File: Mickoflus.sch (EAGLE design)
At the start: 46 parts, among them IC1 74HC595D, IC2 74HC595D

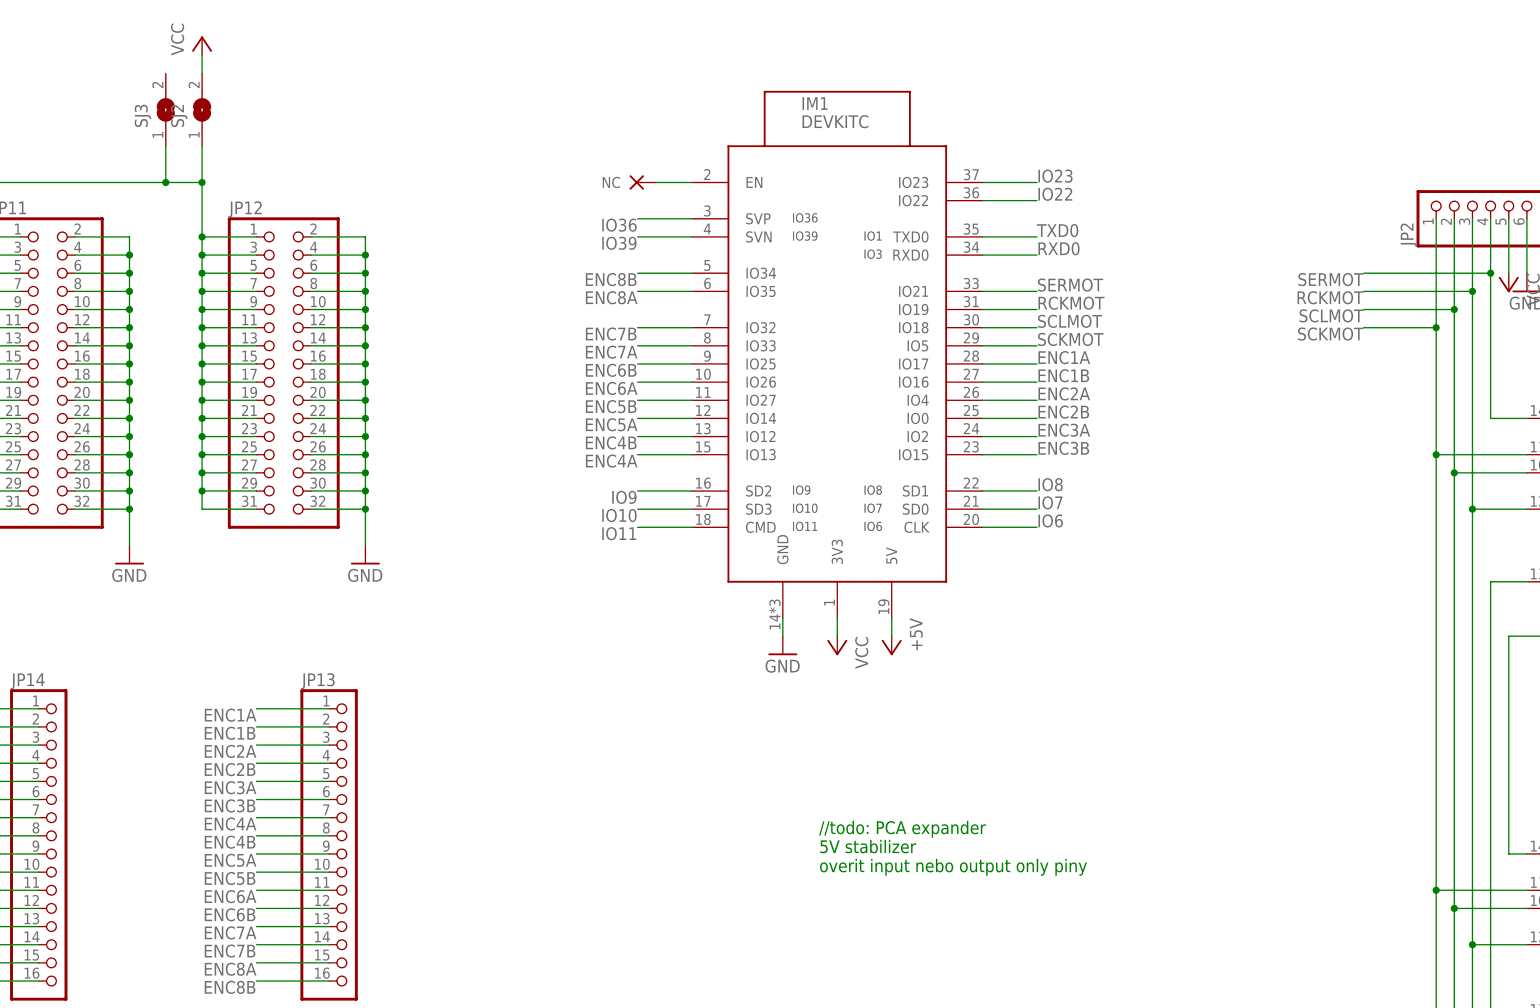
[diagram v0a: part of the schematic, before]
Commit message: Added 5V supply (still no stabilizer from battery to 5V).
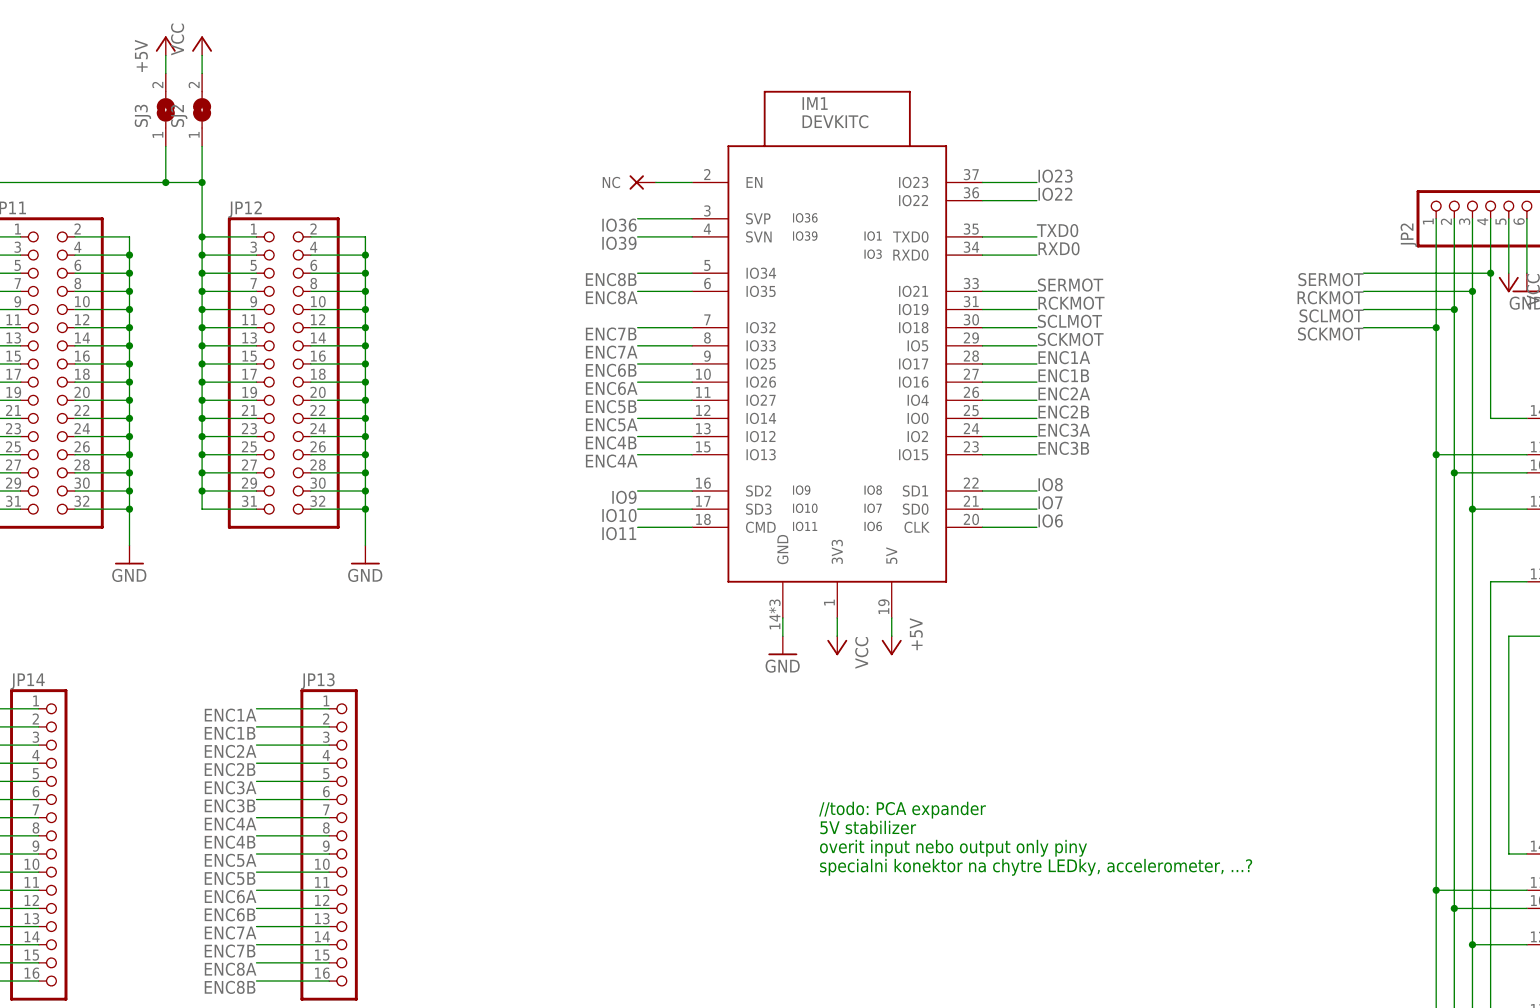
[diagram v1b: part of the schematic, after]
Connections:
- net +5V: now also SJ3.2
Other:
- note added: "//todo: PCA expander 5V stabilizer overit input nebo output only piny specialni konektor na chytre LEDky, accelerometer, ...?"
- note removed: "//todo: PCA expander 5V stabilizer overit input nebo output only piny"
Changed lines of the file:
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@@
 <part name="JP14" library="pinhead" deviceset="PINHD-1X16" device=""/>
 <part name="P+17" library="supply1" deviceset="+5V" device=""/>
+<part name="P+16" library="supply1" deviceset="+5V" device=""/>
 </parts>
 <sheets>
@@
 <text x="-121.92" y="22.86" size="1.778" layer="91">//todo: PCA expander
 5V stabilizer
-overit input nebo output only piny</text>
+overit input nebo output only piny
+specialni konektor na chytre LEDky, accelerometer, ...?</text>
 </plain>
 <instances>
@@
 <instance part="JP14" gate="A" x="-228.6" y="27.94"/>
 <instance part="P+17" gate="1" x="-111.76" y="53.34" rot="R180"/>
+<instance part="P+16" gate="1" x="-213.36" y="139.7"/>
 </instances>
 <busses>
@@
 <wire x1="-111.76" y1="55.88" x2="-111.76" y2="58.42" width="0.1524" layer="91"/>
 </segment>
-</net>
+<segment>
+<pinref part="SJ3" gate="1" pin="2"/>
+<pinref part="P+16" gate="1" pin="+5V"/>
+<wire x1="-213.36" y1="134.62" x2="-213.36" y2="137.16" width="0.1524" layer="91"/>
+</segment>
+</net>

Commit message: Major schematic improvements changed power supply names: VCC -> +3V3, V+ -> VCC fixed encoder power (+3V3 -> +5V) changed ESP pinout (disconnected internal memory pins, moved encoders out of bootstrap pins) ESP reset also resets motors drivers
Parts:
- removed NC1, NC2, NC3, NC4, NC8: NC, NC:NC
- added C1, C2: 100n, rcl_upravena:C-EUC1206
- added D1: (no value), diode:DIODE-0805
- added JP15, JP16, JP17, JP18: (no value), pinhead:PINHD-1X1
- added NC10, NC11, NC5, NC6, NC7, NC9: NC, NC:NC
- added Q1: (no value), transistors:N-MOSFET-SOT23-GSD
- added R1, R2, R3: 10k, rcl_upravena:R-EU_R1206
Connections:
- removed net IO10: IM1.SD3, JP14.7
- removed net IO11: IM1.CMD, JP14.8
- removed net IO6: IM1.CLK, JP14.3
- removed net IO7: IM1.SD0, JP14.4
- removed net IO8: IM1.SD1, JP14.5
- removed net IO9: IM1.SD2, JP14.6
- removed net N$104: NC1.NC, U$4.ULT
- removed net N$105: NC2.NC, U$3.ULT
- removed net N$106: NC3.NC, U$2.ULT
- removed net N$107: NC8.NC, U$1.ULT
- removed net N$56: IM1.EN, NC4.NC
- removed net SCLMOT: IC1A.SCL, IC2A.SCL, IM1.IO18, JP2.2, JP3.5
- removed net V+: POWER1-1.KL, POWER2-1.KL, U$1.VCC, U$2.VCC, U$3.VCC, U$4.VCC
- new net !FAULT0: JP15.1, U$1.ULT
- new net !FAULT1: JP16.1, U$2.ULT
- new net !FAULT2: JP17.1, U$3.ULT
- new net !FAULT3: JP18.1, U$4.ULT
- new net +3V3: C1.1, C2.1, IC1P.VCC, IC2P.VCC, IM1.3V3, JP2.6, JP3.1, Q1.G, R1.2, R3.2, SJ2.2
- new net EN: IC1A.SCL, IC2A.SCL, IM1.EN, JP2.2, JP3.5, Q1.S, R3.1, U$1.!SLEEP, U$2.!SLEEP, U$3.!SLEEP, U$4.!SLEEP
- new net IO10_NC: IM1.SD3, NC6.NC
- new net IO11_NC: IM1.CMD, NC7.NC
- new net IO21: IM1.IO21
- new net IO6_NC: IM1.CLK, NC9.NC
- new net IO7_NC: IM1.SD0, NC10.NC
- new net IO8_NC: IM1.SD1, NC11.NC
- new net IO9_NC: IM1.SD2, NC5.NC
- new net _EN_: D1.C, Q1.D
- net +5V: now also JP1.4, JP10.4, JP4.4, JP5.4, JP6.4, JP7.4, JP8.4, JP9.4
- net ENC1A: now also IM1.IO19; no longer IM1.IO17
- net ENC1B: now also IM1.IO18; no longer IM1.IO16
- net ENC2A: now also IM1.IO5; no longer IM1.IO4
- net ENC2B: now also IM1.IO17; no longer IM1.IO0
- net ENC3A: now also IM1.IO16; no longer IM1.IO2
- net ENC3B: now also IM1.IO4; no longer IM1.IO15
- net GND: now also C1.2, C2.2, IC1P.GND, IC2P.GND, JP1.3, JP10.3, JP2.5, JP3.2, JP4.3, JP5.3, JP6.3, JP7.3, JP8.3, JP9.3, R2.1; no longer JP1.4, JP10.4, JP2.6, JP3.1, JP4.4, JP5.4, JP6.4, JP7.4, JP8.4, JP9.4
- net RCKMOT: now also D1.A, IM1.IO0, R1.1; no longer IM1.IO19
- net SCKMOT: now also IM1.IO15; no longer IM1.IO5
- net SERMOT: now also IM1.IO2, R2.2; no longer IM1.IO21
- net VCC: now also POWER1-1.KL, POWER2-1.KL, U$1.VCC, U$2.VCC, U$3.VCC, U$4.VCC; no longer IM1.3V3, JP1.3, JP10.3, JP2.5, JP3.2, JP4.3, JP5.3, JP6.3, JP7.3, JP8.3, JP9.3, SJ2.2, U$1.!SLEEP, U$2.!SLEEP, U$3.!SLEEP, U$4.!SLEEP
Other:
- note added: "MUSI BYT ZDE!"
- moved on the sheet: IM1, JP11, JP12, JP13, JP14, JP3, SJ2, SJ3

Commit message: Added voltage regulator and IO expander.
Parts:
- added D2: 1N4004, diode:1N4004
- added IC4: (no value), v-reg:78XXS
- added JP19: (no value), pinhead:PINHD-1X4
- added R4, R5: (no value), resistor:R-EU_R1206
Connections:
- new net N$5: D2.C, IC4.IN
- new net SCL: IM1.IO22, JP19.1, R4.1
- new net SDA: IM1.IO23, JP19.2, R5.1
- net +3V3: now also JP19.3, R4.2, R5.2
- net +5V: now also IC4.OUT
- net GND: now also IC4.GND, JP19.4
- net IO22: no longer IM1.IO22
- net IO23: no longer IM1.IO23
- net VCC: now also D2.A
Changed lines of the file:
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@@
 <?xml version="1.0" encoding="utf-8"?>
 <!DOCTYPE eagle SYSTEM "eagle.dtd">
-<eagle version="7.7.0">
+<eagle version="6.5.0">
 <drawing>
 <settings>
@@
 <part name="JP17" library="pinhead" deviceset="PINHD-1X1" device=""/>
 <part name="JP18" library="pinhead" deviceset="PINHD-1X1" device=""/>
+<part name="IC4" library="v-reg" deviceset="78XXS" device=""/>
+<part name="GND30" library="supply1" deviceset="GND" device=""/>
+<part name="P+12" library="supply1" deviceset="VCC" device=""/>
+<part name="P+13" library="supply1" deviceset="+5V" device=""/>
+<part name="D2" library="diode" deviceset="1N4004" device=""/>
+<part name="JP19" library="pinhead" deviceset="PINHD-1X4" device=""/>
+<part name="GND29" library="supply1" deviceset="GND" device=""/>
+<part name="+3V9" library="supply1" deviceset="+3V3" device=""/>
+<part name="R4" library="resistor" deviceset="R-EU_" device="R1206"/>
+<part name="R5" library="resistor" deviceset="R-EU_" device="R1206"/>
+<part name="+3V10" library="supply1" deviceset="+3V3" device=""/>
 </parts>
 <sheets>
@@
 <instance part="JP17" gate="G$1" x="109.22" y="33.02"/>
 <instance part="JP18" gate="G$1" x="109.22" y="2.54"/>
+<instance part="IC4" gate="1" x="-137.16" y="12.7"/>
+<instance part="GND30" gate="1" x="-137.16" y="0"/>
+<instance part="P+12" gate="VCC" x="-170.18" y="20.32"/>
+<instance part="P+13" gate="1" x="-124.46" y="20.32"/>
+<instance part="D2" gate="1" x="-157.48" y="12.7"/>
+<instance part="JP19" gate="A" x="-132.08" y="-20.32"/>
+<instance part="GND29" gate="1" x="-142.24" y="-27.94"/>
+<instance part="+3V9" gate="G$1" x="-142.24" y="-7.62"/>
+<instance part="R4" gate="G$1" x="-193.04" y="-7.62" rot="R90"/>
+<instance part="R5" gate="G$1" x="-187.96" y="-7.62" rot="R90"/>
+<instance part="+3V10" gate="G$1" x="-190.5" y="5.08"/>
 </instances>
 <busses>
@@
 <wire x1="-63.5" y1="78.74" x2="-63.5" y2="81.28" width="0.1524" layer="91"/>
 </segment>
+<segment>
+<pinref part="GND30" gate="1" pin="GND"/>
+<pinref part="IC4" gate="1" pin="GND"/>
+<wire x1="-137.16" y1="2.54" x2="-137.16" y2="5.08" width="0.1524" layer="91"/>
+</segment>
+<segment>
+<pinref part="GND29" gate="1" pin="GND"/>
+<pinref part="JP19" gate="A" pin="4"/>
+<wire x1="-142.24" y1="-25.4" x2="-142.24" y2="-22.86" width="0.1524" layer="91"/>
+<wire x1="-142.24" y1="-22.86" x2="-134.62" y2="-22.86" width="0.1524" layer="91"/>
+</segment>
 </net>
 <net name="N$2" class="0">
@@
 <net name="IO23" class="0">
 <segment>
-<pinref part="IM1" gate="G$1" pin="IO23"/>
-<wire x1="-114.3" y1="111.76" x2="-106.68" y2="111.76" width="0.1524" layer="91"/>
-<label x="-106.68" y="111.76" size="1.778" layer="95"/>
-</segment>
-<segment>
 <pinref part="JP14" gate="A" pin="10"/>
 <wire x1="-246.38" y1="22.86" x2="-256.54" y2="22.86" width="0.1524" layer="91"/>
@@
 </net>
 <net name="IO22" class="0">
-<segment>
-<pinref part="IM1" gate="G$1" pin="IO22"/>
-<wire x1="-114.3" y1="109.22" x2="-106.68" y2="109.22" width="0.1524" layer="91"/>
-<label x="-106.68" y="109.22" size="1.778" layer="95"/>
-</segment>
 <segment>
 <pinref part="JP14" gate="A" pin="9"/>
@@
 <wire x1="215.9" y1="114.3" x2="215.9" y2="124.46" width="0.1524" layer="91"/>
 </segment>
+<segment>
+<pinref part="IC4" gate="1" pin="OUT"/>
+<pinref part="P+13" gate="1" pin="+5V"/>
+<wire x1="-129.54" y1="12.7" x2="-124.46" y2="12.7" width="0.1524" layer="91"/>
+<wire x1="-124.46" y1="12.7" x2="-124.46" y2="17.78" width="0.1524" layer="91"/>
+</segment>
 </net>
 <net name="IO9_NC" class="0">
@@
 <pinref part="R3" gate="G$1" pin="2"/>
 <wire x1="-63.5" y1="152.4" x2="-63.5" y2="147.32" width="0.1524" layer="91"/>
+</segment>
+<segment>
+<pinref part="JP19" gate="A" pin="3"/>
+<pinref part="+3V9" gate="G$1" pin="+3V3"/>
+<wire x1="-134.62" y1="-20.32" x2="-142.24" y2="-20.32" width="0.1524" layer="91"/>
+<wire x1="-142.24" y1="-20.32" x2="-142.24" y2="-10.16" width="0.1524" layer="91"/>
+</segment>
+<segment>
+<pinref part="R4" gate="G$1" pin="2"/>
+<wire x1="-193.04" y1="-2.54" x2="-193.04" y2="0" width="0.1524" layer="91"/>
+<wire x1="-193.04" y1="0" x2="-190.5" y2="0" width="0.1524" layer="91"/>
+<pinref part="R5" gate="G$1" pin="2"/>
+<wire x1="-190.5" y1="0" x2="-187.96" y2="0" width="0.1524" layer="91"/>
+<wire x1="-187.96" y1="0" x2="-187.96" y2="-2.54" width="0.1524" layer="91"/>
+<pinref part="+3V10" gate="G$1" pin="+3V3"/>
+<wire x1="-190.5" y1="2.54" x2="-190.5" y2="0" width="0.1524" layer="91"/>
+<junction x="-190.5" y="0"/>
 </segment>
 </net>
@@
 <wire x1="-66.04" y1="-17.78" x2="-66.04" y2="-15.24" width="0.1524" layer="91"/>
 <pinref part="P+11" gate="VCC" pin="VCC"/>
+</segment>
+<segment>
+<pinref part="P+12" gate="VCC" pin="VCC"/>
+<wire x1="-170.18" y1="12.7" x2="-170.18" y2="17.78" width="0.1524" layer="91"/>
+<pinref part="D2" gate="1" pin="A"/>
+<wire x1="-170.18" y1="12.7" x2="-160.02" y2="12.7" width="0.1524" layer="91"/>
 </segment>
 </net>
@@
 </segment>
 </net>
+<net name="N$5" class="0">
+<segment>
+<pinref part="D2" gate="1" pin="C"/>
+<pinref part="IC4" gate="1" pin="IN"/>
+<wire x1="-154.94" y1="12.7" x2="-144.78" y2="12.7" width="0.1524" layer="91"/>
+</segment>
+</net>
+<net name="SDA" class="0">
+<segment>
+<pinref part="JP19" gate="A" pin="2"/>
+<wire x1="-134.62" y1="-17.78" x2="-149.86" y2="-17.78" width="0.1524" layer="91"/>
+<label x="-149.86" y="-17.78" size="1.778" layer="95"/>
+</segment>
+<segment>
+<pinref part="IM1" gate="G$1" pin="IO23"/>
+<wire x1="-114.3" y1="111.76" x2="-106.68" y2="111.76" width="0.1524" layer="91"/>
+<label x="-106.68" y="111.76" size="1.778" layer="95"/>
+</segment>
+<segment>
+<pinref part="R5" gate="G$1" pin="1"/>
+<wire x1="-187.96" y1="-12.7" x2="-187.96" y2="-17.78" width="0.1524" layer="91"/>
+<label x="-187.96" y="-17.78" size="1.778" layer="95"/>
+</segment>
+</net>
+<net name="SCL" class="0">
+<segment>
+<pinref part="JP19" gate="A" pin="1"/>
+<wire x1="-134.62" y1="-15.24" x2="-149.86" y2="-15.24" width="0.1524" layer="91"/>
+<label x="-149.86" y="-15.24" size="1.778" layer="95"/>
+</segment>
+<segment>
+<pinref part="IM1" gate="G$1" pin="IO22"/>
+<wire x1="-114.3" y1="109.22" x2="-106.68" y2="109.22" width="0.1524" layer="91"/>
+<label x="-106.68" y="109.22" size="1.778" layer="95"/>
+</segment>
+<segment>
+<pinref part="R4" gate="G$1" pin="1"/>
+<wire x1="-193.04" y1="-12.7" x2="-193.04" y2="-17.78" width="0.1524" layer="91"/>
+<label x="-193.04" y="-17.78" size="1.778" layer="95"/>
+</segment>
+</net>
